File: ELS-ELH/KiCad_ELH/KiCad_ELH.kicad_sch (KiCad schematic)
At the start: 9 parts

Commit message: some progress
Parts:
- added J3: Screw_Terminal_01x12, symbol Connector:Screw_Terminal_01x12
- added J4, J5, J6, J7: Screw_Terminal_01x02, symbol Connector:Screw_Terminal_01x02
- added MOSFET1, MOSFET2, MOSFET3, MOSFET5: IRFZ44N, symbol ELH_Library:IRFZ44N
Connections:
- new net: J6.1 (Pin_1), MOSFET2.2 (Drain)
- new net: J5.1 (Pin_1), MOSFET1.2 (Drain)
- new net: J7.1 (Pin_1), MOSFET3.2 (Drain)
- new net: J4.1 (Pin_1), MOSFET5.2 (Drain)

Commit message: Some progress
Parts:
- removed ESP32-S3: ESP32-S3-DevKitC-1, ELH_Library:ESP32-S3-DevKitC-1, symbol ELH_Library:ESP32-S3-DevKitC-1
- removed J3: Screw_Terminal_01x12, symbol Connector:Screw_Terminal_01x12
- removed J4, J5, J6, J7: Screw_Terminal_01x02, symbol Connector:Screw_Terminal_01x02
- removed MOSFET1, MOSFET2, MOSFET3, MOSFET5: IRFZ44N, symbol ELH_Library:IRFZ44N
- added BOOST1: XL6009, ELH_Library:XL6009 Boost, symbol ELH_Library:XL6009_Boost
- added Bornera1: Bornera Boost, ELH_Library:Bornera 2P, symbol Connector:Screw_Terminal_01x02
- added Bornera2: Bornera PT, ELH_Library:Bornera 2P, symbol Connector:Screw_Terminal_01x02
- added ESP1: ESP32 DEVKIT V1, ELH_Library:ESP32 DEVKIT V1, symbol ELH_Library:ESP32 DEVKIT V1
- added MOSFET1: IRLZ44N, ELH_Library:IRLZ44N, symbol ELH_Library:IRFZ44N_1
- added Regulator1: LM1117T, symbol ELH_Library:LM1117T
- added Regulator3: MP1584, symbol ELH_Library:MP1584
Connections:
- net GND: now also BOOST1.4 (OUT-), Bornera2.2 (Pin_2), Regulator1.3 (GND)
- net SPI2_SCK: now reaches IMU1.3 (SCL/SCLK)
- net SPI2_SCK: now also SD_Adapter1.4 (CLK), ESP1.11 (D14)
- net SPI2_MOSI: now reaches IMU1.4 (SDA/SDI)
- net SPI2_MOSI: now also SD_Adapter1.3 (MOSI), ESP1.13 (D13)
- net SPI2_MISO: now reaches IMU1.7 (ADO/SDO)
- net SPI2_MISO: now also SD_Adapter1.5 (MISO), ESP1.12 (D12)
- net CS_IMURaw: now reaches IMU1.9 (NCS)
- net CS_IMURaw: now also ESP1.10 (D27)
- net UART3_RX: now reaches GPS1.2 (TX)
- net UART3_RX: now also ESP1.2 (36/VP)
- net UART3_TX: now reaches GPS1.3 (RX)
- net UART3_TX: now also ESP1.6 (D32)
- net UART1_TX: now reaches Teensy3.0 (RX1)
- net UART1_TX: now also ESP1.8 (D25)
- net UART1_RX: now reaches Teensy3.1 (TX1)
- net UART1_RX: now also ESP1.4 (D34)
- net MOS3: now reaches Teensy3.2 (OUT2)
- net MOS4: now reaches Teensy3.3 (LRCLK2)
- net CS_FLASH: now reaches W25QXX1.2 (CS)
- net CS_FLASH: now also ESP1.23 (D5)
- net SPI1_MISO: now reaches W25QXX1.3 (DO)
- net SPI1_MISO: now also BME2.5 (SDO), ESP1.25 (D19)
- net SPI1_SCK: now reaches W25QXX1.5 (CLK)
- net SPI1_SCK: now also BME2.4 (SCK), ESP1.24 (D18)
- net SPI1_MOSI: now reaches W25QXX1.6 (DI)
- net SPI1_MOSI: now also BME2.6 (SDI), ESP1.30 (D23)
- net CS_SD: now reaches SD_Adapter1.2 (CS)
- net CS_SD: now also ESP1.19 (D2)
- net I2C1_SCL: now reaches IMU3.3 (SCL/RX)
- net I2C1_SCL: now also ESP1.29 (D22)
- net I2C1_SDA: now reaches IMU3.4 (SDA/TX)
- net I2C1_SDA: now also ESP1.26 (D21)
- net CS_ALT: now reaches BME2.7 (CS)
- net CS_ALT: now also ESP1.18 (D15)
- net ADC_VCC: now reaches ADC1.10 (VDD)
- net I2C2_SDA: now reaches ADC1.7 (SDA)
- net I2C2_SDA: now also ESP1.21 (D16)
- net I2C2_SCL: now reaches ADC1.8 (SCL)
- net I2C2_SCL: now also ESP1.22 (D17)
- net ADC_GND: now reaches ADC1.9 (GND)
- new net: BOOST1.1 (IN+), Bornera1.2 (Pin_2)
- new net: BOOST1.2 (IN-), Bornera1.1 (Pin_1)
- new net +5V: BOOST1.3 (OUT+), Bornera2.1 (Pin_1), Regulator1.1 (Input)
- new net MOS1: ESP1.7 (D33)
- new net MOS2: ESP1.20 (D4)
- new net UART2_RX: ESP1.5 (D35)
- new net UART2_TX: ESP1.9 (D26)

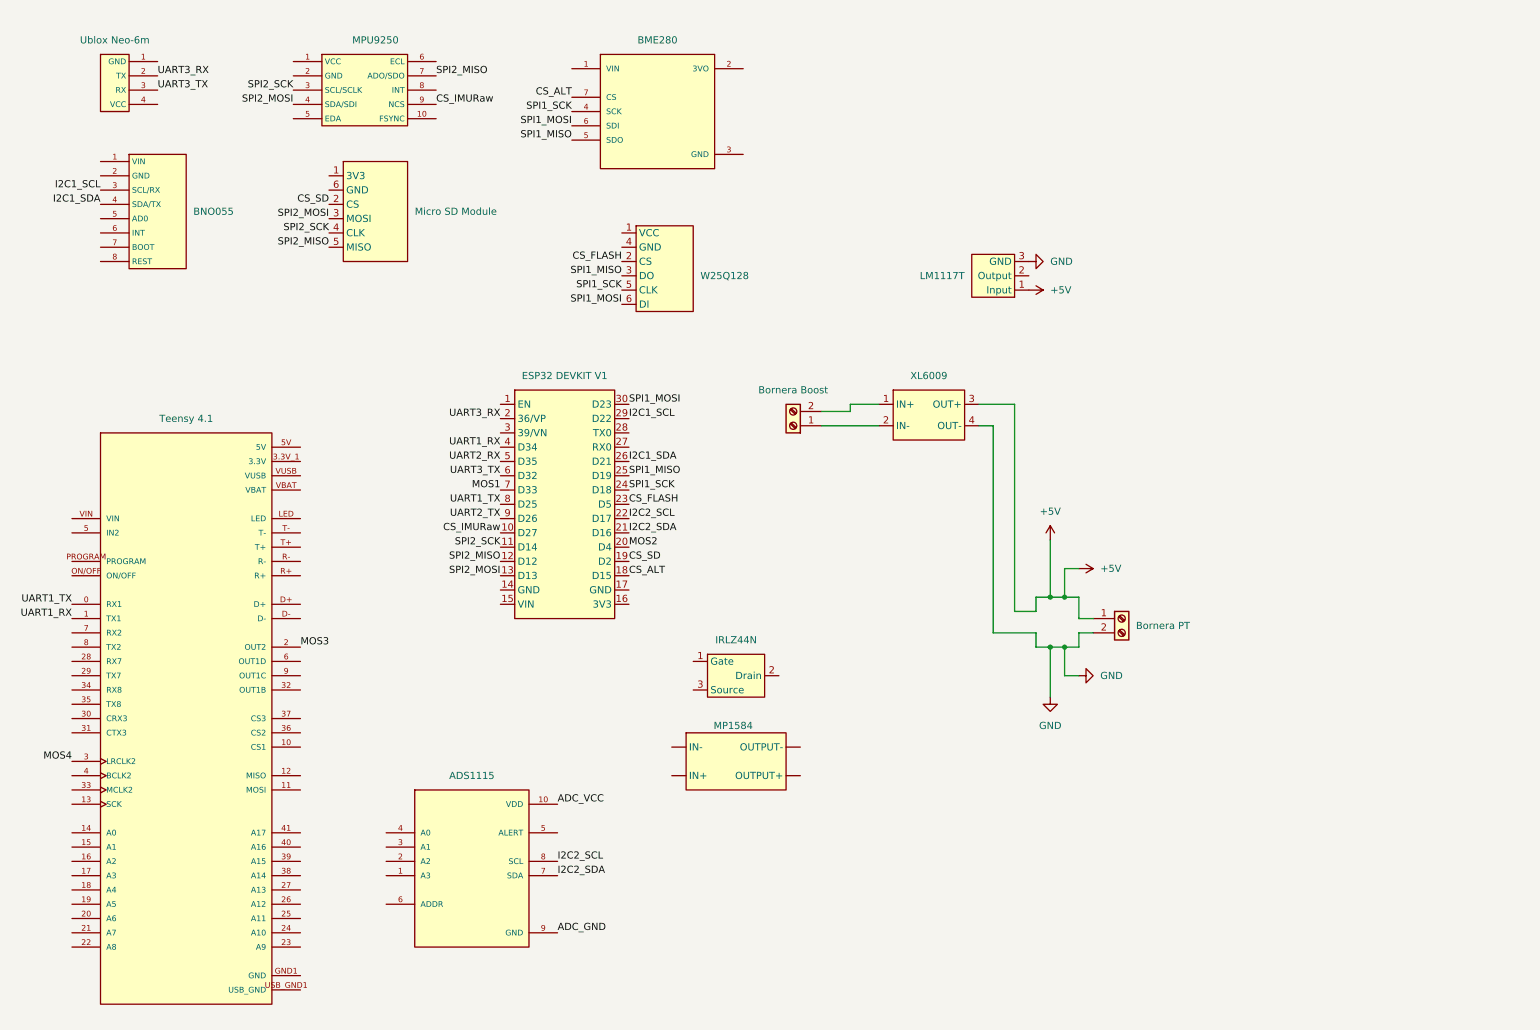
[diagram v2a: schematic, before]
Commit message: Preliminary final schematics
All that's left is to add capacitors and make any other necessary changes.
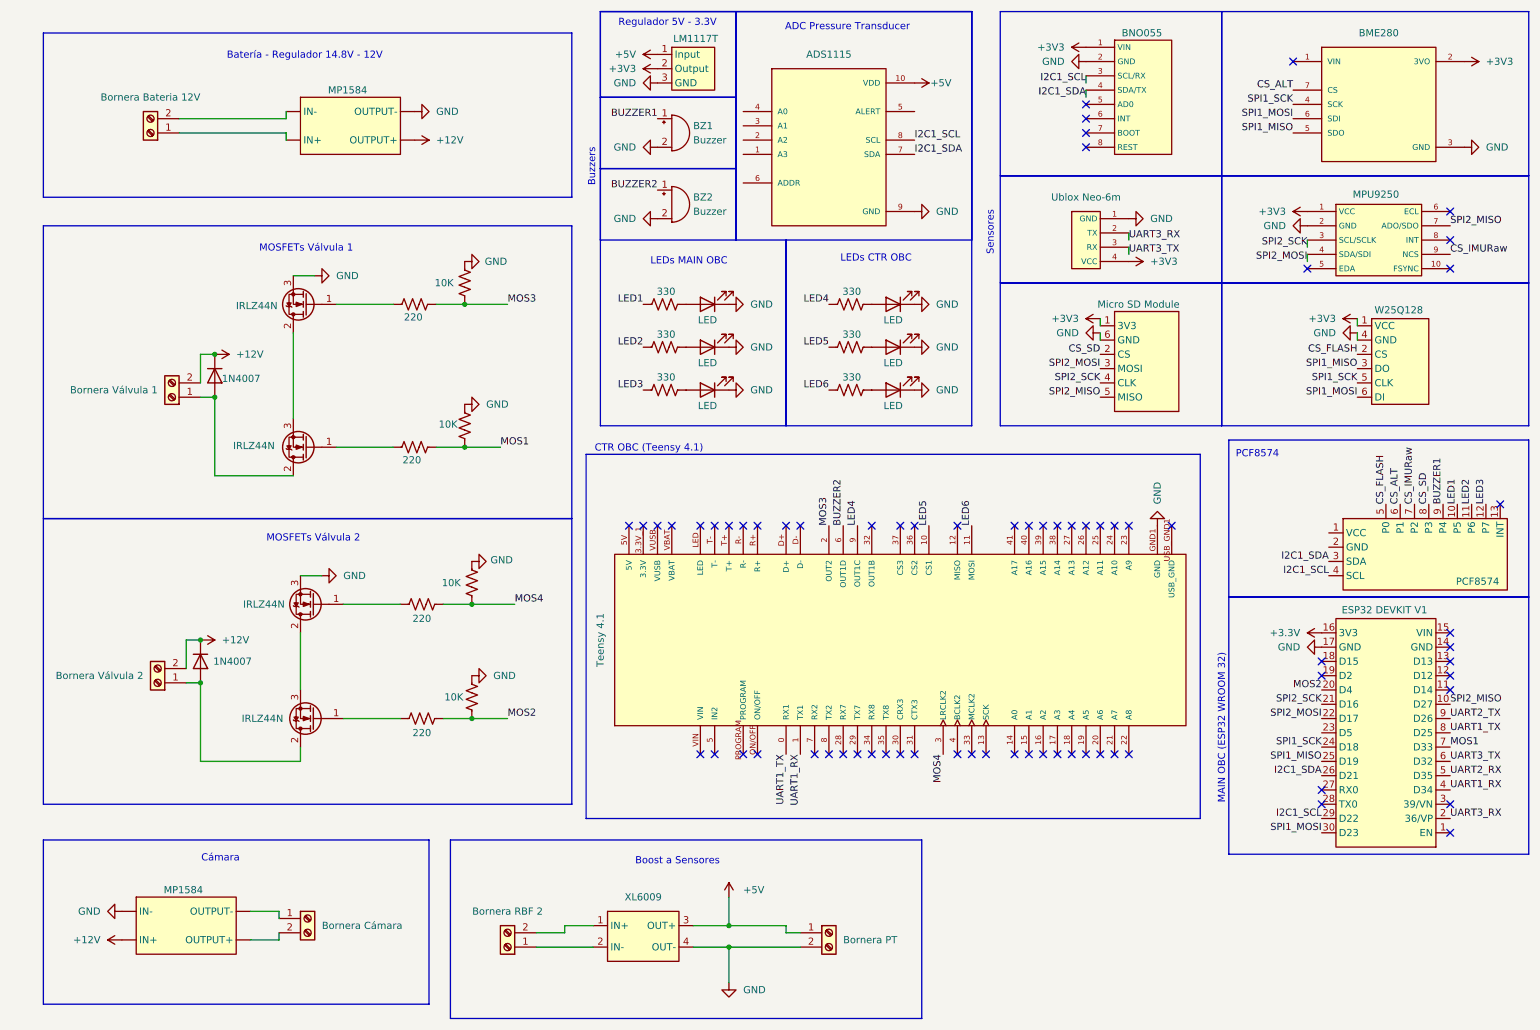
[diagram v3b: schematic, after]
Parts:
- removed MOSFET1: IRLZ44N, ELH_Library:IRLZ44N, symbol ELH_Library:IRFZ44N_1
- removed Regulator3: MP1584, symbol ELH_Library:MP1584
- added Adapter1: PCF8574, ELH_Library:PCF8574, symbol ELH_Library:PCF8574
- added BZ1, BZ2: Buzzer, Buzzer_Beeper:Buzzer_12x9.5RM7.6, symbol Device:Buzzer
- added Bornera3: Bornera Cámara, ELH_Library:Bornera 2P, symbol Connector:Screw_Terminal_01x02
- added Bornera4: Bornera Válvula 1, ELH_Library:Bornera 2P, symbol Connector:Screw_Terminal_01x02
- added Bornera6: Bornera Bateria 12V, ELH_Library:Bornera 2P, symbol Connector:Screw_Terminal_01x02
- added Bornera7: Bornera Válvula 2, ELH_Library:Bornera 2P, symbol Connector:Screw_Terminal_01x02
- added D1, D3: 1N4007, Diode_THT:D_DO-41_SOD81_P10.16mm_Horizontal, symbol Diode:1N4007
- added D2, D4, D5, D6, D7, D8: LED, ELH_Library:LED, symbol Device:LED
- added Q1, Q3, Q4, Q5: IRLZ44N, Package_TO_SOT_THT:TO-220-3_Vertical, symbol Transistor_FET:IRLZ44N
- added R1, R11, R6, R9: 220, Resistor_THT:R_Axial_DIN0207_L6.3mm_D2.5mm_P7.62mm_Horizontal, symbol Device:R_US
- added R10, R2, R3, R8: 10K, Resistor_THT:R_Axial_DIN0207_L6.3mm_D2.5mm_P7.62mm_Horizontal, symbol Device:R_US
- added R12, R13, R14, R4, R5, R7: 330, Resistor_THT:R_Axial_DIN0207_L6.3mm_D2.5mm_P7.62mm_Horizontal, symbol Device:R_US
- added Regulator2, Regulator4: MP1584, symbol ELH_Library:MP1584
- Bornera1: value Bornera Boost -> Bornera RBF 2
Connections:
- net ADC_GND is gone; now on net GND: ADC1.9 (GND)
- net ADC_VCC is gone; now on net +5V: ADC1.10 (VDD)
- net CS_ALT: now also Adapter1.6 (P1); no longer ESP1.18 (D15)
- net CS_FLASH: now also Adapter1.5 (P0); no longer ESP1.23 (D5)
- net CS_IMURaw: now also Adapter1.7 (P2); no longer ESP1.10 (D27)
- net CS_SD: now also Adapter1.8 (P3); no longer ESP1.19 (D2)
- net GND: now also BME2.3 (GND), ESP1.17 (GND), GPS1.1 (GND), IMU1.2 (GND), IMU3.2 (GND), SD_Adapter1.6 (GND), W25QXX1.4 (GND), BZ1.2 (-), BZ2.2 (-), D2.1 (K), D4.1 (K), D5.1 (K), D6.1 (K), D7.1 (K), D8.1 (K), Q4.3 (S), Q5.3 (S), R10.1, R2.1, R3.2, R8.2, Regulator2. (OUTPUT+), Regulator4. (OUTPUT+)
- net I2C1_SCL: now also ADC1.8 (SCL), Adapter1.4 (SCL)
- net I2C1_SDA: now also ADC1.7 (SDA), Adapter1.3 (SDA)
- net MOS1: now also R3.1, R6.1
- net MOS2: now also R8.1, R9.1
- net MOS3: now also R10.2, R11.2
- net MOS4: now also R1.2, R2.2
- net SPI2_MISO: now also ESP1.10 (D27); no longer ESP1.12 (D12)
- net SPI2_MOSI: now also ESP1.22 (D17); no longer ESP1.13 (D13)
- net SPI2_SCK: now also ESP1.21 (D16); no longer ESP1.11 (D14)
- net +3V3: now reaches IMU1.1 (VCC)
- net +3V3: now also BME2.2 (3VO), GPS1.4 (VCC), IMU3.1 (VIN), Regulator1.2 (Output), SD_Adapter1.1 (3V3), W25QXX1.1 (VCC)
- net LED5: now reaches Teensy3.10 (CS1)
- net LED5: now also R13.2
- net LED6: now reaches Teensy3.11 (MOSI)
- net LED6: now also R14.2
- net BUZZER2: now reaches Teensy3.6 (OUT1D)
- net BUZZER2: now also BZ2.1 (+)
- net LED4: now reaches Teensy3.9 (OUT1C)
- net LED4: now also R12.2
- net +3.3V: now reaches ESP1.16 (3V3)
- removed net I2C2_SCL: ADC1.8 (SCL), ESP1.22 (D17)
- removed net I2C2_SDA: ADC1.7 (SDA), ESP1.21 (D16)
- new net: D8.2 (A), R14.1
- new net: D2.2 (A), R4.1
- new net: D4.2 (A), R5.1
- new net: D7.2 (A), R13.1
- new net: Q5.1 (G), R1.1
- new net: Q3.3 (S), Q5.2 (D)
- new net: Bornera7.1 (Pin_1), D3.2 (A), Q3.2 (D)
- new net: D5.2 (A), R7.1
- new net: Q3.1 (G), R9.2
- new net: D6.2 (A), R12.1
- new net: Bornera3.1 (Pin_1), Regulator4. (OUTPUT+)
- new net: Bornera3.2 (Pin_2), Regulator4. (OUTPUT+)
- new net: Bornera6.1 (Pin_1), Regulator2. (OUTPUT+)
- new net: Bornera6.2 (Pin_2), Regulator2. (OUTPUT+)
- new net: Q4.1 (G), R11.1
- new net: Bornera4.1 (Pin_1), D1.2 (A), Q1.2 (D)
- new net: Q1.1 (G), R6.2
- new net: Q1.3 (S), Q4.2 (D)
- new net +12V: Bornera4.2 (Pin_2), Bornera7.2 (Pin_2), D1.1 (K), D3.1 (K), Regulator2. (OUTPUT+), Regulator4. (OUTPUT+)
- new net BUZZER1: Adapter1.9 (P4), BZ1.1 (+)
- new net LED1: Adapter1.10 (P5), R4.2
- new net LED2: Adapter1.11 (P6), R5.2
- new net LED3: Adapter1.12 (P7), R7.2
- no-connect marks 0 -> 70
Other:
- note added: "ADC Pressure Transducer"
- note added: "Batería - Regulador 14.8V - 12V"
- note added: "Boost a Sensores"
- note added: "Buzzers"
- note added: "CTR OBC (Teensy 4.1)"
- note added: "Cámara"
- note added: "LEDs CTR OBC"
- note added: "LEDs MAIN OBC"
- note added: "MAIN OBC (ESP32 WROOM 32)"
- note added: "MOSFETs Válvula 1"
- note added: "MOSFETs Válvula 2"
- note added: "PCF8574"
- note added: "Regulador 5V - 3.3V"
- note added: "Sensores"

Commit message: Finished schematics
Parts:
- removed Bornera2: Bornera PT, ELH_Library:Bornera 2P, symbol Connector:Screw_Terminal_01x02
- removed D2, D4, D5, D6, D7, D8: LED, ELH_Library:LED, symbol Device:LED
- removed D3: 1N4007, Diode_THT:D_DO-41_SOD81_P10.16mm_Horizontal, symbol Diode:1N4007
- removed Q3, Q5: IRLZ44N, Package_TO_SOT_THT:TO-220-3_Vertical, symbol Transistor_FET:IRLZ44N
- removed R13, R14: 330, Resistor_THT:R_Axial_DIN0207_L6.3mm_D2.5mm_P7.62mm_Horizontal, symbol Device:R_US
- added Bornera5: RCS 1 Screw Terminal, ELH_Library:Bornera 2P, symbol Connector:Screw_Terminal_01x02
- added C1, C2, C4, C6, C8: 100nF, symbol Device:C_Small
- added C10, C9: 47uF, symbol Device:C_Small
- added C3, C5, C7: 100uF, symbol Device:C_Small
- added D10, D3: LED_RKGB, LED_THT:LED_D5.0mm-4_RGB_Staggered_Pins, symbol Device:LED_RKGB
- added D9: 1N4007, Diode_THT:D_DO-41_SOD81_P10.16mm_Horizontal, symbol Diode:1N4007
- added J1: Pressure Transducer Screw Terminal, symbol Connector:Screw_Terminal_01x03
- added Q2, Q6: IRLZ44N, Package_TO_SOT_THT:TO-220-3_Vertical, symbol Transistor_FET:IRLZ44N
- added R16, R20: 220, Resistor_THT:R_Axial_DIN0207_L6.3mm_D2.5mm_P7.62mm_Horizontal, symbol Device:R_US
- added R18, R19: 10K, Resistor_THT:R_Axial_DIN0207_L6.3mm_D2.5mm_P7.62mm_Horizontal, symbol Device:R_US
- Bornera1: value Bornera RBF 2 -> Sensor Power Supply Screw Terminal
- Bornera3: value Bornera Cámara -> Camera Screw Terminal
- Bornera4: value Bornera Válvula 1 -> RCS 2 Screw Terminal
- Bornera6: value Bornera Bateria 12V -> Actuator Power Supply Screw Terminal
- Bornera7: value Bornera Válvula 2 -> COM Camera Screw Terminal
- R1: value 220 -> 330
- R11: value 220 -> 10K
- R12: value 330 -> 220
- R2, R8: value 10K -> 330
- R3: value 10K -> 220
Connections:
- net +12V: now also Bornera5.2 (Pin_2), C10.1, C7.1, C8.1, C9.1, D9.1 (K); no longer Bornera7.2 (Pin_2)
- net +5V: now also ESP1.15 (VIN), Teensy3.VIN, C1.2, C2.2, J1.1 (Pin_1)
- net BUZZER1: now also R12.1; no longer BZ1.1 (+)
- net BUZZER2: now also R9.1; no longer BZ2.1 (+)
- net GND: now also ESP1.14 (GND), R10.2, R11.2, C1.1, C2.1, C7.2, C8.2, D10.2 (K), D3.2 (K), J1.2 (Pin_2), Q2.3 (S), R18.2, R19.2; no longer ESP1.17 (GND), R10.1, R2.1, R3.2, R8.2
- net LED4: now also R8.2; no longer R12.2
- net LED5: now also R2.2
- net LED6: now also R1.2
- net MOS1: now also R16.1; no longer R3.1, R6.1
- net MOS2: now also R6.1; no longer R8.1, R9.1
- net MOS3: now also R20.1; no longer R10.2, R11.2
- net MOS4: now also R3.1; no longer R1.2, R2.2
- net UART2_RX: now also Bornera7.2 (Pin_2)
- net UART2_TX: now also Bornera7.1 (Pin_1)
- net at BOOST1.1 (IN+), Bornera1.2 (Pin_2): now also C5.2, C6.2
- net at BOOST1.2 (IN-), Bornera1.1 (Pin_1): now also C5.1, C6.1
- net at R4.1: now also D10.1 (RA)
- net at R5.1: now also D10.3 (GA)
- net at R1.1: now also D3.4 (BA)
- net at R7.1: now also D10.4 (BA)
- net at R9.2: now also BZ2.1 (+)
- net at Bornera6.1 (Pin_1), Regulator2. (OUTPUT+): now also C3.1, C4.1
- net at Bornera6.2 (Pin_2), Regulator2. (OUTPUT+): now also C3.2, C4.2
- net at Q4.1 (G), R11.1: now also R3.2
- net at Bornera4.1 (Pin_1), D1.2 (A), Q1.2 (D): now also C10.2
- net at Q1.1 (G), R6.2: now also R10.1
- net PT_ADC: now reaches ADC1.4 (A0)
- net PT_ADC: now also J1.3 (Pin_3)
- new net: Q6.1 (G), R16.2, R18.1
- new net: Bornera5.1 (Pin_1), C9.2, D9.2 (A), Q6.2 (D)
- new net: Q2.1 (G), R19.1, R20.2
- new net: D3.1 (RA), R8.1
- new net: D3.3 (GA), R2.1
- new net: Q2.2 (D), Q6.3 (S)
- new net: BZ1.1 (+), R12.2
- no-connect marks 70 -> 67
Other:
- note added: "BUZZER CTR OBC"
- note added: "BUZZER MAIN OBC"
- note added: "Circuit for the MOSFETs of Solenoid Valve 1"
- note added: "Circuit for the MOSFETs of Solenoid Valve 2"
- note added: "Power Supply"
- note added: "Regulator 5V - 3.3V"
- note added: "Voltage Boost Circuit for Sensors"
- note added: "Voltage Regulator Circuit for Actuators"
- note added: "Voltage Regulator Circuit for a Camera"
- note removed: "ADC Pressure Transducer"
- note removed: "Batería - Regulador 14.8V - 12V"
- note removed: "Boost a Sensores"
- note removed: "Buzzers"
- note removed: "Cámara"
- note removed: "MOSFETs Válvula 1"
- note removed: "MOSFETs Válvula 2"
- note removed: "Regulador 5V - 3.3V"
- note removed: "Sensores"
